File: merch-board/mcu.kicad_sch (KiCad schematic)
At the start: 26 parts, among them SW1 BOOTSEL, SW2 RESET, U2 W25Q128JVS, U3 RP2040, Y1 ABM8-272-T3

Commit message: Add LCSC part numbers
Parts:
- C10, C11, C12, C3, C4, C5, C6, C7, C8, C9: LCSC (none) -> C1525
- C13, C14: LCSC (none) -> C1548
- C15, C16: LCSC (none) -> C14445
- R2, R6: LCSC (none) -> C11702
- R4, R5: LCSC (none) -> C25100
- SW1, SW2: LCSC (none) -> C318884
- TP1, TP2: now left out of the parts list
- U2: LCSC (none) -> C113767
- U3: LCSC (none) -> C2040
- Y1: LCSC (none) -> C20625731
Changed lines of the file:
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@@
+			)
+		)
+		(property "LCSC" "C2040"
+			(at 215.9 111.76 0)
+			(effects
+				(font
+					(size 1.27 1.27)
+				)
+				(hide yes)
 			)
 		)
@@
 		(property "Description" "128Mbit / 16MiB Serial Flash Memory, Standard/Dual/Quad SPI, 2.7-3.6V, SOIC-8"
 			(at 97.79 82.55 0)
+			(effects
+				(font
+					(size 1.27 1.27)
+				)
+				(hide yes)
+			)
+		)
+		(property "LCSC" "C113767"
+			(at 97.79 110.49 0)
 			(effects
 				(font
@@
 			)
 		)
+		(property "LCSC" "C1525"
+			(at 104.14 83.82 0)
+			(effects
+				(font
+					(size 1.27 1.27)
+				)
+				(hide yes)
+			)
+		)
 		(pin "1"
 		)
@@
 			)
 		)
+		(property "LCSC" "C25100"
+			(at 171.45 81.28 90)
+			(effects
+				(font
+					(size 1.27 1.27)
+				)
+				(hide yes)
+			)
+		)
 		(pin "1"
 		)
@@
 			)
 		)
+		(property "LCSC" "C25100"
+			(at 171.45 86.36 90)
+			(effects
+				(font
+					(size 1.27 1.27)
+				)
+				(hide yes)
+			)
+		)
 		(pin "1"
 		)
@@
 			)
 		)
+		(property "LCSC" "C1525"
+			(at 68.58 38.1 0)
+			(effects
+				(font
+					(size 1.27 1.27)
+				)
+				(hide yes)
+			)
+		)
 		(pin "1"
 		)
@@
 			)
 		)
+		(property "LCSC" "C1525"
+			(at 80.01 38.1 0)
+			(effects
+				(font
+					(size 1.27 1.27)
+				)
+				(hide yes)
+			)
+		)
 		(pin "1"
 		)
@@
 			)
 		)
+		(property "LCSC" "C1525"
+			(at 91.44 38.1 0)
+			(effects
+				(font
+					(size 1.27 1.27)
+				)
+				(hide yes)
+			)
+		)
 		(pin "1"
 		)
@@
 			)
 		)
+		(property "LCSC" "C1525"
+			(at 102.87 38.1 0)
+			(effects
+				(font
+					(size 1.27 1.27)
+				)
+				(hide yes)
+			)
+		)
 		(pin "1"
 		)
@@
 			)
 		)
+		(property "LCSC" "C1525"
+			(at 114.3 38.1 0)
+			(effects
+				(font
+					(size 1.27 1.27)
+				)
+				(hide yes)
+			)
+		)
 		(pin "1"
 		)
@@
 			)
 		)
+		(property "LCSC" "C1525"
+			(at 125.73 38.1 0)
+			(effects
+				(font
+					(size 1.27 1.27)
+				)
+				(hide yes)
+			)
+		)
 		(pin "1"
 		)
@@
 			)
 		)
+		(property "LCSC" "C1525"
+			(at 137.16 38.1 0)
+			(effects
+				(font
+					(size 1.27 1.27)
+				)
+				(hide yes)
+			)
+		)
 		(pin "1"
 		)
@@
 			)
 		)
+		(property "LCSC" "C1525"
+			(at 33.02 38.1 0)
+			(effects
+				(font
+					(size 1.27 1.27)
+				)
+				(hide yes)
+			)
+		)
 		(pin "1"
 		)
@@
 			)
 		)
+		(property "LCSC" "C1525"
+			(at 44.45 38.1 0)
+			(effects
+				(font
+					(size 1.27 1.27)
+				)
+				(hide yes)
+			)
+		)
 		(pin "1"
 		)
@@
 			)
 		)
+		(property "LCSC" "C14445"
+			(at 201.93 58.42 0)
+			(effects
+				(font
+					(size 1.27 1.27)
+				)
+				(hide yes)
+			)
+		)
 		(pin "1"
 		)
@@
 			)
 		)
+		(property "LCSC" "C14445"
+			(at 234.95 59.69 0)
+			(effects
+				(font
+					(size 1.27 1.27)
+				)
+				(hide yes)
+			)
+		)
 		(pin "1"
 		)
@@
 			)
 		)
+		(property "LCSC" "C318884"
+			(at 31.75 134.62 90)
+			(effects
+				(font
+					(size 1.27 1.27)
+				)
+				(hide yes)
+			)
+		)
 		(pin "1"
 		)
@@
 			)
 		)
+		(property "LCSC" "C20625731"
+			(at 160.02 124.46 90)
+			(effects
+				(font
+					(size 1.27 1.27)
+				)
+				(hide yes)
+			)
+		)
 		(pin "1"
 		)
@@
 			)
 		)
+		(property "LCSC" "C1548"
+			(at 144.78 119.38 0)
+			(effects
+				(font
+					(size 1.27 1.27)
+				)
+				(hide yes)
+			)
+		)
 		(pin "1"
 		)
@@
 			)
 		)
+		(property "LCSC" "C11702"
+			(at 48.26 102.87 90)
+			(effects
+				(font
+					(size 1.27 1.27)
+				)
+				(hide yes)
+			)
+		)
 		(pin "1"
 		)
@@
 			)
 		)
+		(property "LCSC" "C11702"
+			(at 172.72 129.54 90)
+			(effects
+				(font
+					(size 1.27 1.27)
+				)
+				(hide yes)
+			)
+		)
 		(pin "1"
 		)
@@
 		(unit 1)
 		(exclude_from_sim no)
-		(in_bom yes)
+		(in_bom no)
 		(on_board yes)
 		(dnp no)
@@
 			)
 		)
+		(property "LCSC" "C318884"
+			(at 31.75 107.95 90)
+			(effects
+				(font
+					(size 1.27 1.27)
+				)
+				(hide yes)
+			)
+		)
 		(pin "1"
 		)
@@
 			)
 		)
+		(property "LCSC" "C1548"
+			(at 144.78 129.54 0)
+			(effects
+				(font
+					(size 1.27 1.27)
+				)
+				(hide yes)
+			)
+		)
 		(pin "1"
 		)
@@
 		(unit 1)
 		(exclude_from_sim no)
-		(in_bom yes)
-		(on_board yes)
-		(dnp no)
+		(in_bom no)
+		(on_board yes)
+		(dnp no)

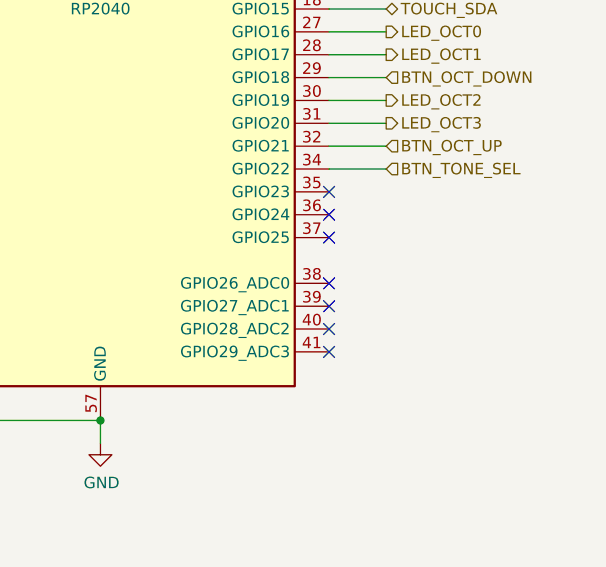
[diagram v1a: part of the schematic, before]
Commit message: Add volume pot to schematic
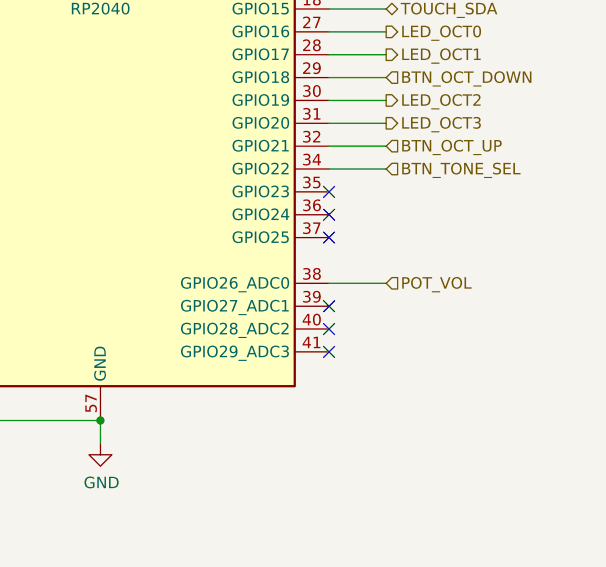
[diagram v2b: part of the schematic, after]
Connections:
- net POT_VOL: now reaches U3.38 (GPIO26_ADC0)
- no-connect marks 15 -> 14
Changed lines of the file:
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@@
-	)
-	(no_connect
-		(at 241.3 142.24)
 	)
 	(no_connect
@@
 		(pts
 			(xy 201.93 62.23) (xy 201.93 63.5)
+		)
+		(stroke
+			(width 0)
+			(type default)
+		)
+	)
+	(wire
+		(pts
+			(xy 241.3 142.24) (xy 247.65 142.24)
 		)
 		(stroke
@@
 		(effects
 			(font
+				(size 1.27 1.27)
+			)
+			(justify left)
+		)
+	)
+	(hierarchical_label "POT_VOL"
+		(shape input)
+		(at 247.65 142.24 0)
+		(effects
+			(font

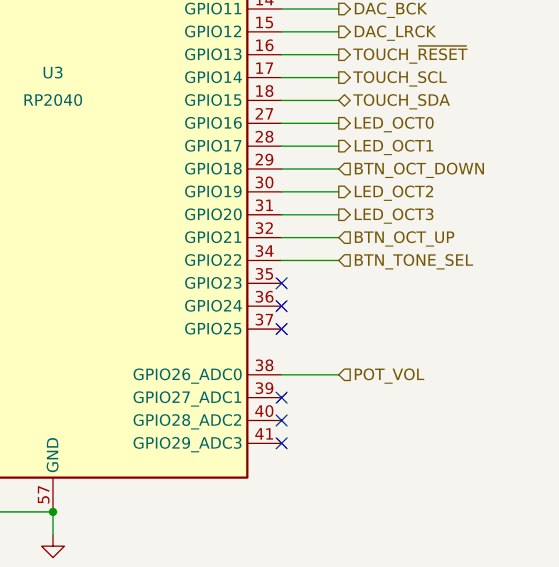
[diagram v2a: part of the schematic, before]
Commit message: Add WS2812B-2020 for tone indicator
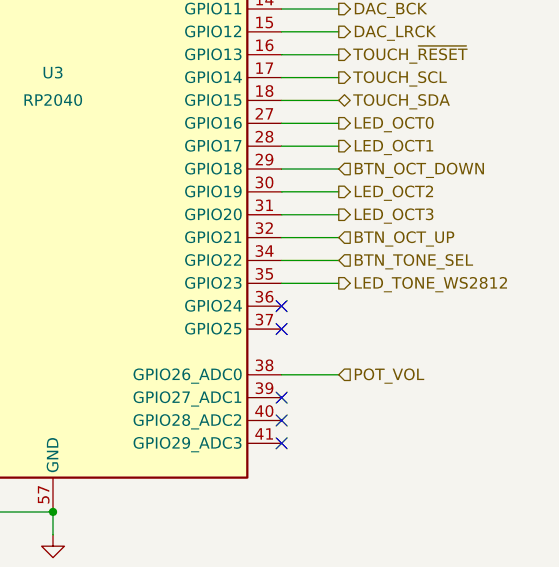
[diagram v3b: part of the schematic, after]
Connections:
- net LED_TONE_WS2812: now reaches U3.35 (GPIO23)
- no-connect marks 14 -> 13
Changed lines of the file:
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@@
-	)
-	(no_connect
-		(at 241.3 132.08)
 	)
 	(no_connect
@@
 		(pts
 			(xy 213.36 64.77) (xy 210.82 64.77)
+		)
+		(stroke
+			(width 0)
+			(type default)
+		)
+	)
+	(wire
+		(pts
+			(xy 241.3 132.08) (xy 247.65 132.08)
 		)
 		(stroke
@@
 		(effects
 			(font
+				(size 1.27 1.27)
+			)
+			(justify left)
+		)
+	)
+	(hierarchical_label "LED_TONE_WS2812"
+		(shape output)
+		(at 247.65 132.08 0)
+		(effects
+			(font

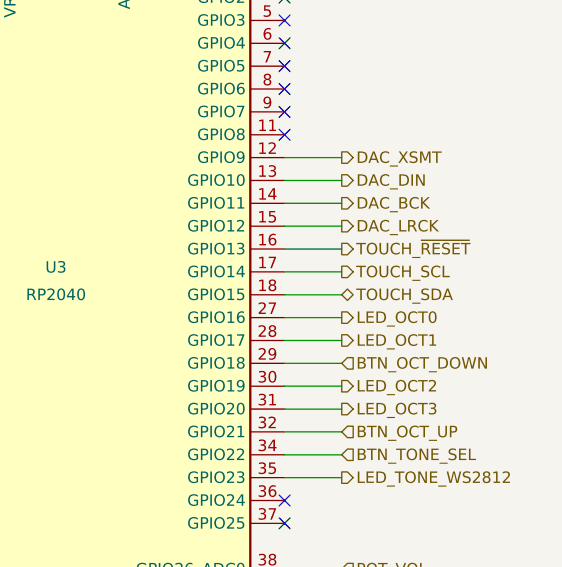
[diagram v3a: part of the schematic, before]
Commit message: Swap I2C pins around and connect 1v1 output to input
* I2C1 pins 14 and 15 have fixed roles
* 1v1 regulator output from rp2040 is not internally connected to DVDD input
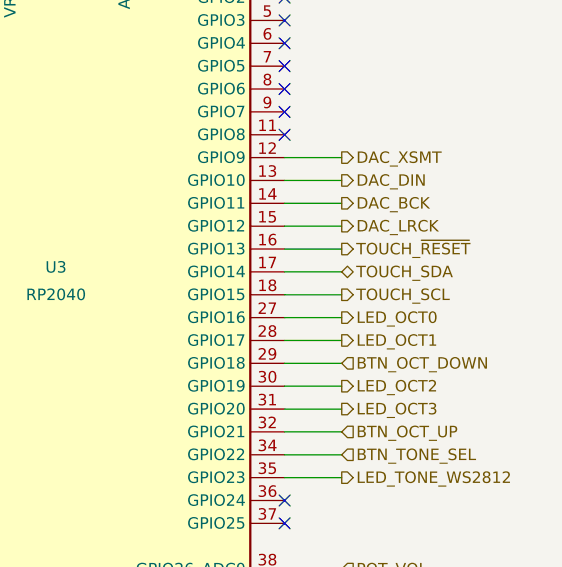
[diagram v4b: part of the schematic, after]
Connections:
- net TOUCH_SCL: now also U3.18 (GPIO15); no longer U3.17 (GPIO14)
- net TOUCH_SDA: now also U3.17 (GPIO14); no longer U3.18 (GPIO15)
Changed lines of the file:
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@@
 	(hierarchical_label "TOUCH_SDA"
 		(shape bidirectional)
-		(at 247.65 111.76 0)
+		(at 247.65 109.22 0)
 		(effects
 			(font
@@
 	(hierarchical_label "TOUCH_SCL"
 		(shape output)
-		(at 247.65 109.22 0)
+		(at 247.65 111.76 0)
 		(effects
 			(font
